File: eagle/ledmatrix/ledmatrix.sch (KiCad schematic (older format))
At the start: 65 parts, among them P1 CONN_01X05, P2 CONN_01X05, Q1 BSS138, Q10 BSS138, Q11 BSS138, Q12 BSS138, Q13 BSS138, Q14 BSS138, Q15 BSS138, Q16 BSS138, Q17 BSS138, Q18 BSS138, Q19 BSS138, Q2 BSS138, Q20 BSS138, Q3 BSS138, Q4 BSS138, Q5 BSS138, Q6 BSS138, Q7 BSS138, Q8 BSS138, Q9 BSS138, U1 74HC595, U2 74HC595, U3 74HC595

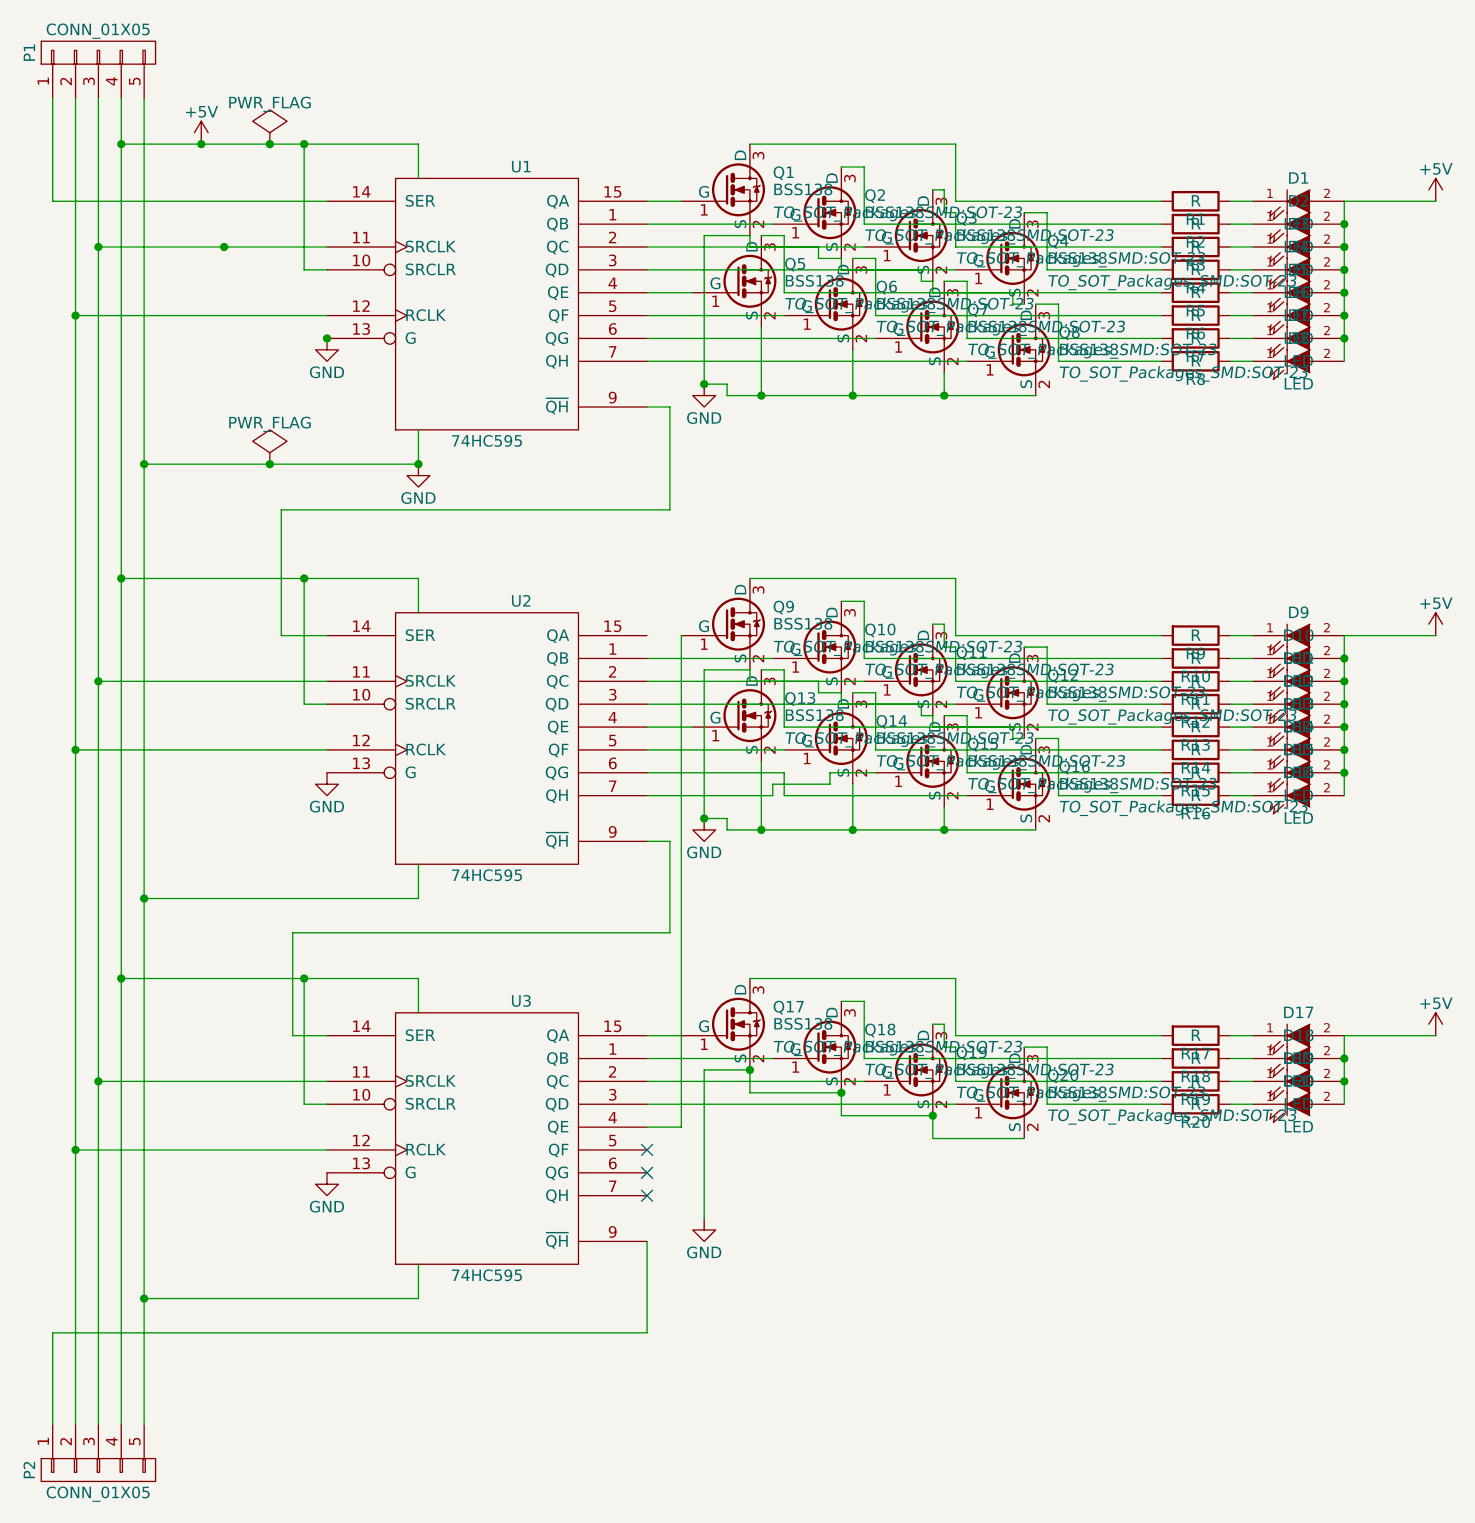
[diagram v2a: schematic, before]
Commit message: more routing -- latch, clock proposal 1
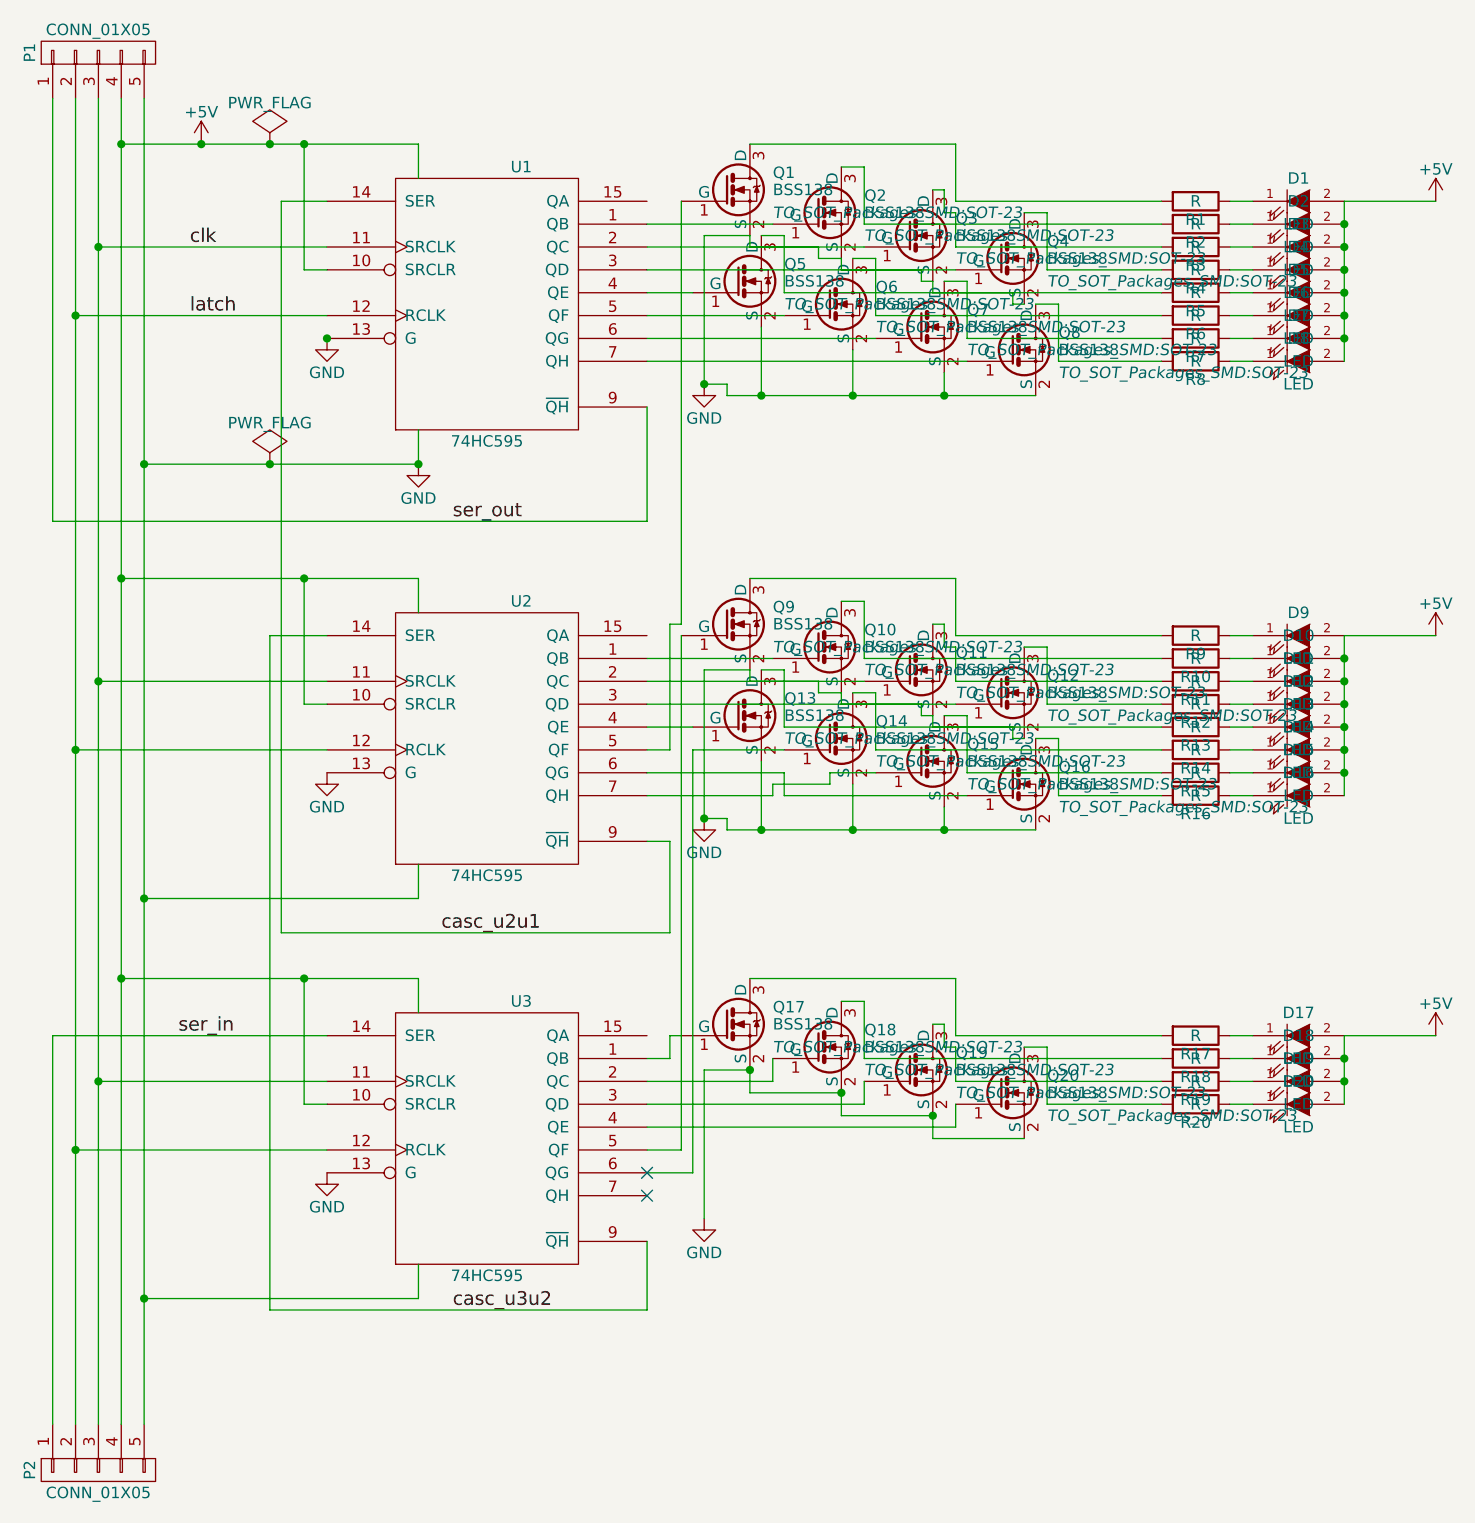
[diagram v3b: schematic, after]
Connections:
- net clk: now reaches P1.3 (P3), P2.3 (P3), U1.11 (SRCLK), U2.11 (SRCLK), U3.11 (SRCLK)
- net latch: now reaches P1.2 (P2), P2.2 (P2), U1.12 (RCLK), U2.12 (RCLK), U3.12 (RCLK)
- net casc_u3u2: now reaches U2.14 (SER)
- net casc_u3u2: now also U3.9 (~QH); no longer U1.9 (~QH)
- net at U2.5 (QF): now also Q1.1 (G); no longer Q14.1 (G)
- net casc_u2u1: now reaches U2.9 (~QH)
- net casc_u2u1: now also U1.14 (SER); no longer U3.14 (SER)
- net ser_out: now reaches P1.1 (P1)
- net ser_out: now also U1.9 (~QH); no longer U1.14 (SER)
- net at U1.15 (QA): no longer Q1.1 (G)
- net at U3.1 (QB): now also Q17.1 (G); no longer Q18.1 (G)
- net at U3.15 (QA): no longer Q17.1 (G)
- net at U3.2 (QC): now also Q18.1 (G); no longer Q19.1 (G)
- net at U3.3 (QD): now also Q19.1 (G); no longer Q20.1 (G)
- net at U3.4 (QE): now also Q20.1 (G); no longer Q9.1 (G)
- net at U3.5 (QF): now also Q9.1 (G)
- net at U3.6 (QG): now also Q14.1 (G)
- net ser_in: now reaches P2.1 (P1)
- net ser_in: now also U3.14 (SER); no longer U3.9 (~QH)
- no-connect marks 3 -> 2
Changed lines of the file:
@@
 $EndComp
 Wire Wire Line
-	3800 2300 3900 2300
-Wire Wire Line
-	3900 2300 3900 2750
-Wire Wire Line
-	3900 2750 2200 2750
-Wire Wire Line
-	2200 2750 2200 3300
-Wire Wire Line
-	2200 3300 2400 3300
+	2200 1400 2200 4600
 Wire Wire Line
 	3800 4200 3900 4200
@@
 	3900 4200 3900 4600
 Wire Wire Line
-	3900 4600 2250 4600
-Wire Wire Line
-	2250 4600 2250 5050
-Wire Wire Line
-	2250 5050 2400 5050
+	3900 4600 2200 4600
 Wire Wire Line
 	1400 1600 2400 1600
@@
 	1400 5250 2400 5250
 Wire Wire Line
-	2800 2400 2800 2550
-Wire Wire Line
-	2800 2550 1600 2550
+	2800 2550 2800 2400
+Wire Wire Line
+	1600 2550 2800 2550
 Wire Wire Line
 	1600 950  1600 6750
@@
 Wire Wire Line
 	1400 950  1400 6750
-Connection ~ 1950 1600
 Wire Wire Line
 	2400 1900 1300 1900
@@
 	1300 5550 2400 5550
 Connection ~ 1300 3800
-Wire Wire Line
-	2400 1400 1200 1400
-Wire Wire Line
-	1200 1400 1200 950
 $Comp
 L BSS138 Q1
@@
 	1    0    0    -1
 $EndComp
-Wire Wire Line
-	3950 5050 3800 5050
 $Comp
 L LED D17
@@
 Wire Wire Line
 	5550 5100 5550 5350
-Wire Wire Line
-	4350 5150 3800 5150
-Wire Wire Line
-	3800 5250 4750 5250
-Wire Wire Line
-	3800 5350 5150 5350
 Connection ~ 6850 5250
 Connection ~ 6850 5150
 Wire Wire Line
 	6850 5050 7250 5050
-Wire Wire Line
-	3950 1400 3800 1400
 $Comp
 L BSS138 Q9
@@
 	0    -1   1    0
 $EndComp
-Wire Wire Line
-	3800 5950 3800 6350
-Wire Wire Line
-	3800 6350 1200 6350
-Wire Wire Line
-	1200 6350 1200 6750
 Connection ~ 1300 5550
 Connection ~ 1400 1600
@@
 Connection ~ 2400 2000
 Connection ~ 2800 2550
-NoConn ~ 3800 5550
 NoConn ~ 3800 5650
 NoConn ~ 3800 5750
@@
 Connection ~ 2150 2550
 Wire Wire Line
-	3950 3300 3950 5450
-Wire Wire Line
-	3950 5450 3800 5450
-Wire Wire Line
-	3800 3800 4400 3800
+	3950 3300 3950 5550
 Wire Wire Line
 	5200 4000 4400 4000
@@
 Wire Wire Line
 	4350 4000 3800 4000
+Wire Wire Line
+	3950 1400 3950 3250
+Wire Wire Line
+	3950 3250 3900 3250
+Wire Wire Line
+	3900 3250 3900 3800
+Wire Wire Line
+	3900 3800 3800 3800
+Wire Wire Line
+	4400 3800 4000 3800
+Wire Wire Line
+	4000 3800 4000 5650
+Wire Wire Line
+	4000 5650 3800 5650
+Wire Wire Line
+	3950 5550 3800 5550
+Wire Wire Line
+	5150 5350 5150 5450
+Wire Wire Line
+	5150 5450 3800 5450
+Wire Wire Line
+	4750 5250 4750 5350
+Wire Wire Line
+	4750 5350 3800 5350
+Wire Wire Line
+	4350 5150 4350 5250
+Wire Wire Line
+	4350 5250 3800 5250
+Wire Wire Line
+	3800 5150 3900 5150
+Wire Wire Line
+	3900 5150 3900 5050
+Wire Wire Line
+	3900 5050 3950 5050
+Text Label 1800 1600 0    60   ~ 0
+clk
+Text Label 1800 1900 0    60   ~ 0
+latch
+Wire Wire Line
+	3800 2300 3800 2800
+Wire Wire Line
+	3800 2800 1200 2800
+Wire Wire Line
+	1200 2800 1200 950
+Wire Wire Line
+	1200 6750 1200 5050
+Wire Wire Line
+	1200 5050 2400 5050
+Text Label 1750 5050 0    60   ~ 0
+ser_in
+Wire Wire Line
+	2200 1400 2400 1400
+Wire Wire Line
+	2400 3300 2150 3300
+Wire Wire Line
+	2150 3300 2150 6250
+Wire Wire Line
+	2150 6250 3800 6250
+Wire Wire Line
+	3800 6250 3800 5950
+Text Label 2950 2800 0    60   ~ 0
+ser_out
+Text Label 2900 4600 0    60   ~ 0
+casc_u2u1
+Text Label 2950 6250 0    60   ~ 0
+casc_u3u2
 $EndSCHEMATC

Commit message: all routed
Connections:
- net clk: now also P1.2 (P2), P2.2 (P2); no longer P1.3 (P3), P2.3 (P3)
- net latch: now also P1.1 (P1), P2.1 (P1); no longer P1.2 (P2), P2.2 (P2)
- net ser_in: now also P2.3 (P3); no longer P2.1 (P1)
- net ser_out: now also P1.3 (P3); no longer P1.1 (P1)
- no-connect marks 2 -> 4
